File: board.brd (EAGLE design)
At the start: 14.2 x 10.2 mm, 7 parts, among them J1 UJC-HP-3-SMT-TR

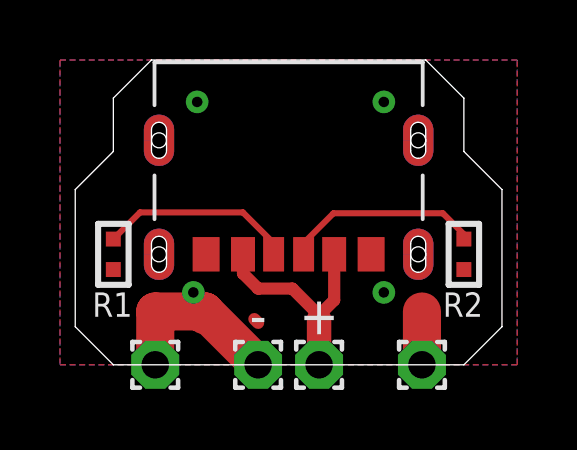
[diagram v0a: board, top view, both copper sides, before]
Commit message: Fix board layout
After receiving my boards, I realized that  the holes are lined up with the bottom of the pad instead of the middle like intended.
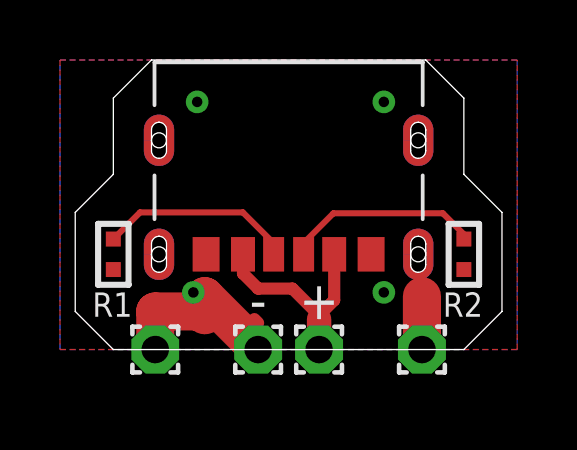
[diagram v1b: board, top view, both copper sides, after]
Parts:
- moved + 0.51 mm to (8.64, 0.51)
- moved - 0.51 mm to (6.60, 0.51)
- moved PAD1 0.51 mm to (3.17, 0.51)
- moved PAD4 0.51 mm to (12.1, 0.51)
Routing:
- net VCC: track 7.70 -> 7.19 mm
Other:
- board size 14.2 x 10.2 mm -> 14.2 x 9.7 mm
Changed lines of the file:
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@@
 <setting verticaltext="up"/>
 </settings>
-<grid distance="0.005" unitdist="inch" unit="inch" style="lines" multiple="1" display="yes" altdistance="0.025" altunitdist="inch" altunit="inch"/>
+<grid distance="0.01" unitdist="inch" unit="inch" style="lines" multiple="1" display="yes" altdistance="0.025" altunitdist="inch" altunit="inch"/>
 <layers>
 <layer number="1" name="Top" color="4" fill="1" visible="yes" active="yes"/>
@@
 vaugerbird</text>
 <wire x1="12.192" y1="10.16" x2="3.048" y2="10.16" width="0" layer="20"/>
-<wire x1="1.778" y1="0" x2="13.462" y2="0" width="0" layer="20"/>
-<wire x1="14.732" y1="1.27" x2="14.732" y2="5.842" width="0" layer="20"/>
-<wire x1="0.508" y1="1.27" x2="0.508" y2="5.842" width="0" layer="20"/>
-<wire x1="1.778" y1="7.112" x2="1.778" y2="8.89" width="0" layer="20"/>
-<wire x1="13.462" y1="7.112" x2="13.462" y2="8.89" width="0" layer="20"/>
-<wire x1="1.778" y1="7.112" x2="0.508" y2="5.842" width="0" layer="20"/>
-<wire x1="13.462" y1="7.112" x2="14.732" y2="5.842" width="0" layer="20"/>
-<wire x1="14.732" y1="1.27" x2="13.462" y2="0" width="0" layer="20"/>
+<wire x1="1.778" y1="0.508" x2="13.462" y2="0.508" width="0" layer="20"/>
+<wire x1="14.732" y1="1.778" x2="14.732" y2="5.08" width="0" layer="20"/>
+<wire x1="0.508" y1="1.778" x2="0.508" y2="5.08" width="0" layer="20"/>
+<wire x1="1.778" y1="6.35" x2="1.778" y2="8.89" width="0" layer="20"/>
+<wire x1="13.462" y1="6.35" x2="13.462" y2="8.89" width="0" layer="20"/>
+<wire x1="1.778" y1="6.35" x2="0.508" y2="5.08" width="0" layer="20"/>
+<wire x1="13.462" y1="6.35" x2="14.732" y2="5.08" width="0" layer="20"/>
 <wire x1="13.462" y1="8.89" x2="12.192" y2="10.16" width="0" layer="20"/>
 <wire x1="3.048" y1="10.16" x2="1.778" y2="8.89" width="0" layer="20"/>
-<wire x1="0.508" y1="1.27" x2="1.778" y2="0" width="0" layer="20"/>
+<wire x1="13.462" y1="0.508" x2="14.732" y2="1.778" width="0" layer="20"/>
+<wire x1="1.778" y1="0.508" x2="0.508" y2="1.778" width="0" layer="20"/>
 </plain>
 <attributes>
@@
 <attribute name="PRICE" value="None" x="-11.43" y="12.573" size="1.778" layer="27" rot="R180" display="off"/>
 </element>
-<element name="PAD1" library="wirepad" library_urn="urn:adsk.eagle:library:412" package="1,6/0,9" package3d_urn="urn:adsk.eagle:package:30840/1" value="" x="3.175" y="0" smashed="yes">
-<attribute name="POPULARITY" value="7" x="20.955" y="-12.7" size="1.778" layer="27" display="off"/>
-<attribute name="VALUE" x="3.175" y="0.6" size="0.0254" layer="27"/>
-</element>
-<element name="+" library="wirepad" library_urn="urn:adsk.eagle:library:412" package="1,6/0,9" package3d_urn="urn:adsk.eagle:package:30840/1" value="" x="8.636" y="0" smashed="yes">
-<attribute name="NAME" x="8.636" y="1.651" size="1.27" layer="25" font="vector" ratio="10" align="center"/>
-<attribute name="POPULARITY" value="7" x="32.766" y="-12.7" size="1.778" layer="27" display="off"/>
-<attribute name="VALUE" x="8.636" y="0.6" size="0.0254" layer="27"/>
-</element>
-<element name="-" library="wirepad" library_urn="urn:adsk.eagle:library:412" package="1,6/0,9" package3d_urn="urn:adsk.eagle:package:30840/1" value="" x="6.604" y="0" smashed="yes">
-<attribute name="NAME" x="6.604" y="1.651" size="1.27" layer="25" font="vector" ratio="10" align="center"/>
-<attribute name="POPULARITY" value="7" x="24.384" y="-17.78" size="1.778" layer="27" display="off"/>
-<attribute name="VALUE" x="6.604" y="0.6" size="0.0254" layer="27"/>
-</element>
-<element name="PAD4" library="wirepad" library_urn="urn:adsk.eagle:library:412" package="1,6/0,9" package3d_urn="urn:adsk.eagle:package:30840/1" value="" x="12.065" y="0" smashed="yes">
-<attribute name="POPULARITY" value="7" x="36.195" y="-17.78" size="1.778" layer="27" display="off"/>
-<attribute name="VALUE" x="12.065" y="0.6" size="0.0254" layer="27"/>
+<element name="PAD1" library="wirepad" library_urn="urn:adsk.eagle:library:412" package="1,6/0,9" package3d_urn="urn:adsk.eagle:package:30840/1" value="" x="3.175" y="0.508" smashed="yes">
+<attribute name="POPULARITY" value="7" x="20.955" y="-12.192" size="1.778" layer="27" display="off"/>
+<attribute name="VALUE" x="3.175" y="1.108" size="0.0254" layer="27"/>
+</element>
+<element name="+" library="wirepad" library_urn="urn:adsk.eagle:library:412" package="1,6/0,9" package3d_urn="urn:adsk.eagle:package:30840/1" value="" x="8.636" y="0.508" smashed="yes">
+<attribute name="NAME" x="8.636" y="2.159" size="1.27" layer="25" font="vector" ratio="10" align="center"/>
+<attribute name="POPULARITY" value="7" x="32.766" y="-12.192" size="1.778" layer="27" display="off"/>
+<attribute name="VALUE" x="8.636" y="1.108" size="0.0254" layer="27"/>
+</element>
+<element name="-" library="wirepad" library_urn="urn:adsk.eagle:library:412" package="1,6/0,9" package3d_urn="urn:adsk.eagle:package:30840/1" value="" x="6.604" y="0.508" smashed="yes">
+<attribute name="NAME" x="6.604" y="2.159" size="1.27" layer="25" font="vector" ratio="10" align="center"/>
+<attribute name="POPULARITY" value="7" x="24.384" y="-17.272" size="1.778" layer="27" display="off"/>
+<attribute name="VALUE" x="6.604" y="1.108" size="0.0254" layer="27"/>
+</element>
+<element name="PAD4" library="wirepad" library_urn="urn:adsk.eagle:library:412" package="1,6/0,9" package3d_urn="urn:adsk.eagle:package:30840/1" value="" x="12.065" y="0.508" smashed="yes">
+<attribute name="POPULARITY" value="7" x="36.195" y="-17.272" size="1.778" layer="27" display="off"/>
+<attribute name="VALUE" x="12.065" y="1.108" size="0.0254" layer="27"/>
 </element>
 <element name="R2" library="rc-master-smd" package="R0402" value="" x="13.462" y="3.683" smashed="yes" rot="R90">
@@
 <wire x1="8.636" y1="1.651" x2="7.747" y2="2.54" width="0.4064" layer="1"/>
 <wire x1="7.747" y1="2.54" x2="6.604" y2="2.54" width="0.4064" layer="1"/>
-<wire x1="8.636" y1="0" x2="8.636" y2="1.524" width="0.8128" layer="1"/>
+<wire x1="8.636" y1="0.508" x2="8.636" y2="1.524" width="0.8128" layer="1"/>
 <wire x1="6.604" y1="2.54" x2="6.1" y2="3.044" width="0.4064" layer="1"/>
 <wire x1="6.1" y1="3.044" x2="6.1" y2="3.683" width="0.4064" layer="1"/>
@@
 <contactref element="PAD4" pad="1"/>
 <contactref element="PAD1" pad="1"/>
-<wire x1="3.175" y1="1.778" x2="3.175" y2="0" width="1.27" layer="1"/>
-<wire x1="12.065" y1="0" x2="12.065" y2="1.778" width="1.27" layer="1"/>
+<wire x1="3.175" y1="1.778" x2="3.175" y2="0.508" width="1.27" layer="1"/>
+<wire x1="12.065" y1="0.508" x2="12.065" y2="2.286" width="1.27" layer="1"/>
 <wire x1="4.826" y1="1.651" x2="4.826" y2="1.778" width="1.27" layer="1"/>
+<wire x1="4.826" y1="1.778" x2="4.826" y2="2.286" width="1.27" layer="1"/>
 <wire x1="4.826" y1="1.778" x2="3.175" y2="1.778" width="1.27" layer="1"/>
 <wire x1="6.604" y1="1.397" x2="6.477" y2="1.524" width="0.4064" layer="1"/>
-<wire x1="6.604" y1="0" x2="4.826" y2="1.778" width="1.27" layer="1"/>
+<wire x1="6.604" y1="0.508" x2="4.826" y2="2.286" width="1.27" layer="1"/>
 <polygon width="0.1524" layer="1" spacing="0.0635">
 <vertex x="0" y="10.16"/>
-<vertex x="0" y="0"/>
-<vertex x="15.24" y="0"/>
+<vertex x="0" y="0.508"/>
+<vertex x="15.24" y="0.508"/>
 <vertex x="15.24" y="10.16"/>
 </polygon>
 <polygon width="0.1524" layer="16">
 <vertex x="15.24" y="10.16"/>
-<vertex x="15.24" y="0"/>
-<vertex x="0" y="0"/>
+<vertex x="15.24" y="0.508"/>
+<vertex x="0" y="0.508"/>
 <vertex x="0" y="10.16"/>
 </polygon>
